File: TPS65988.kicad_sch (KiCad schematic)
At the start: 30 parts, among them J10 USB_C_Receptacle, J11 Conn_01x03, J12 Conn_01x03, J13 Conn_01x04, J9 USB_C_Receptacle, U13 TPS65988

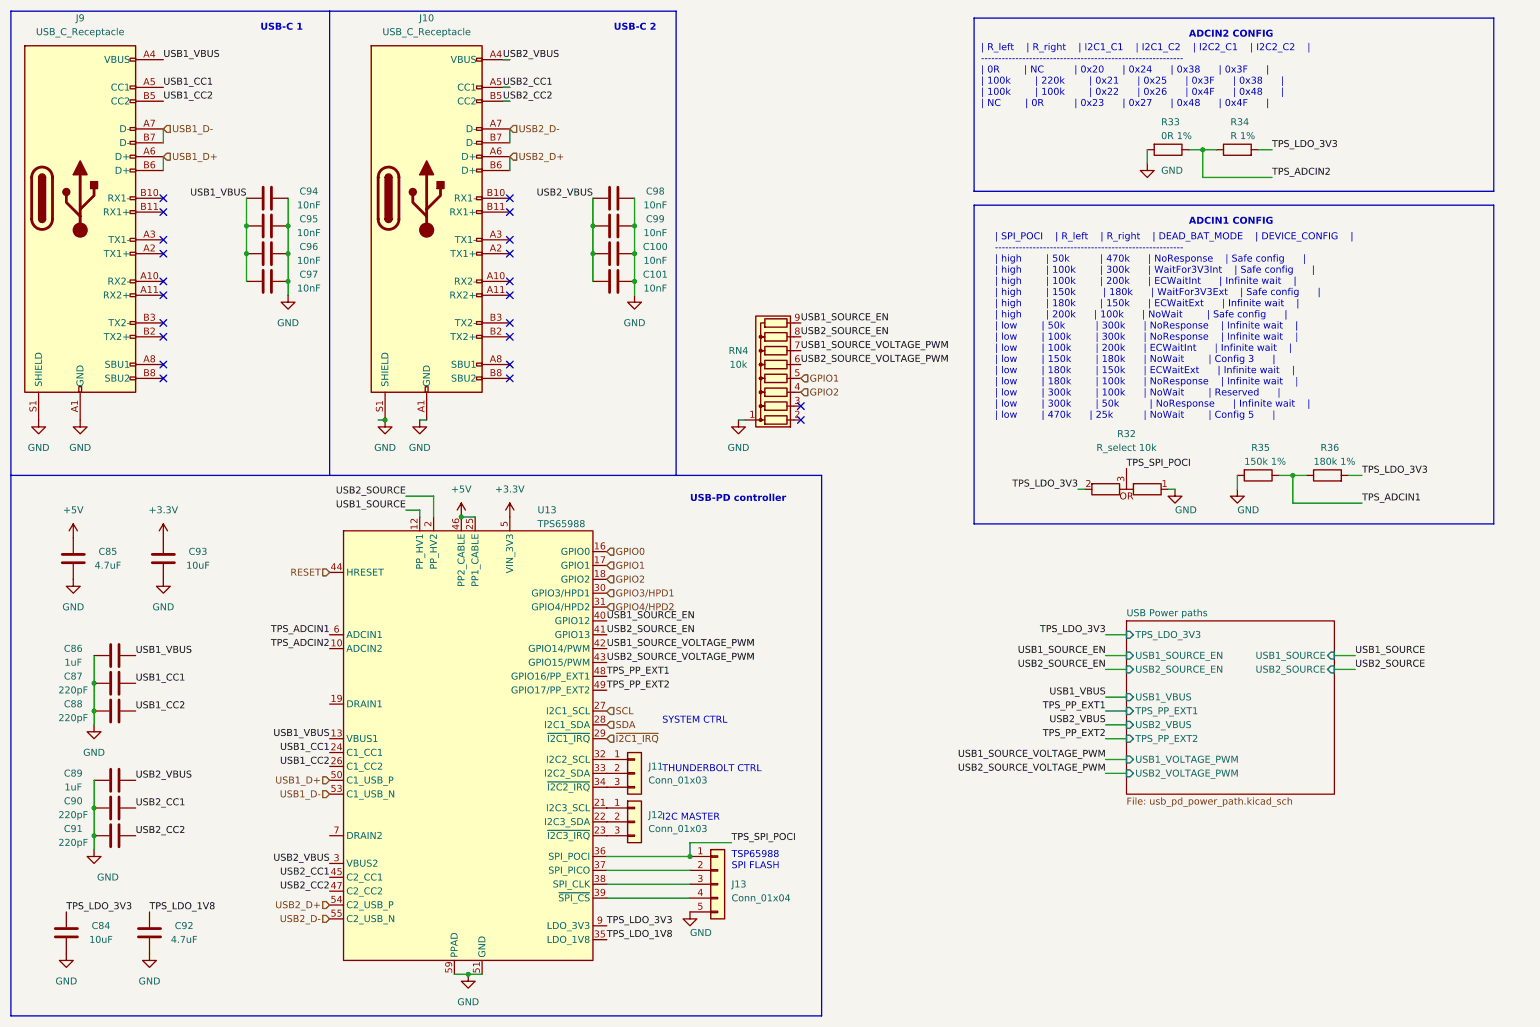
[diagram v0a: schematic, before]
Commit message: added nfc antenna components, added most of footprints
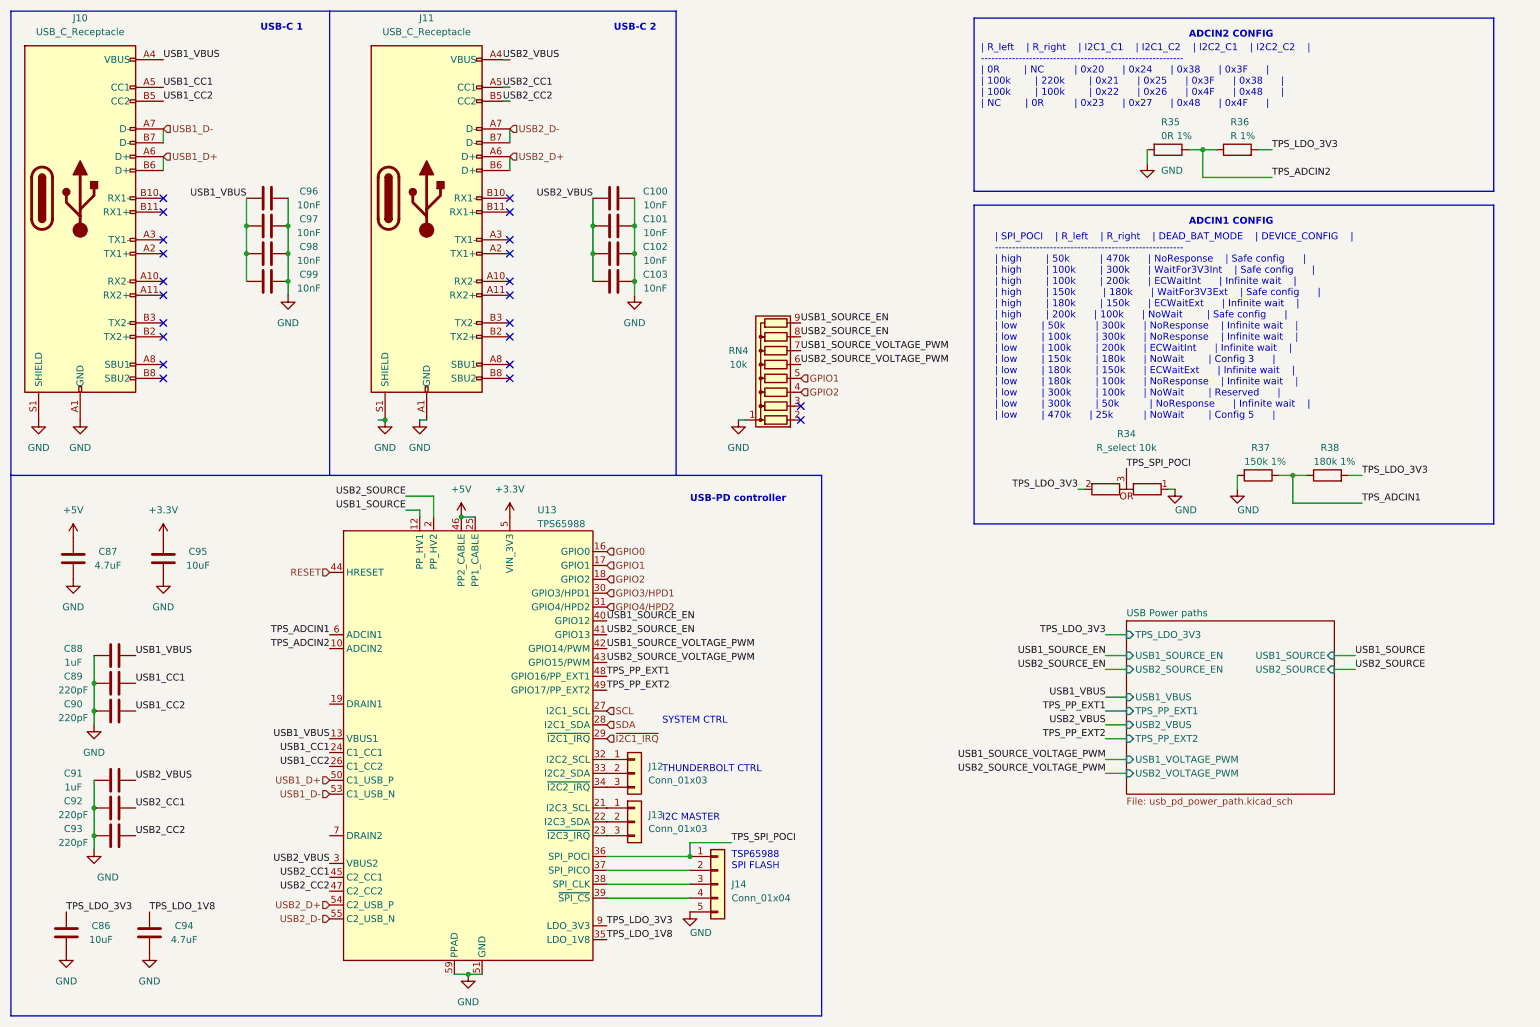
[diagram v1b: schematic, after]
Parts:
- C100: renamed from C98; footprint (none) -> Capacitor_SMD:C_0603_1608Metric_Pad1.08x0.95mm_HandSolder
- C101: renamed from C99; footprint (none) -> Capacitor_SMD:C_0603_1608Metric_Pad1.08x0.95mm_HandSolder
- C102: renamed from C100; footprint (none) -> Capacitor_SMD:C_0603_1608Metric_Pad1.08x0.95mm_HandSolder
- C103: renamed from C101; footprint (none) -> Capacitor_SMD:C_0603_1608Metric_Pad1.08x0.95mm_HandSolder
- C87: renamed from C85; footprint (none) -> Capacitor_SMD:C_0603_1608Metric_Pad1.08x0.95mm_HandSolder
- C88: renamed from C86; footprint (none) -> Capacitor_SMD:C_0603_1608Metric_Pad1.08x0.95mm_HandSolder
- C89: renamed from C87; footprint (none) -> Capacitor_SMD:C_0603_1608Metric_Pad1.08x0.95mm_HandSolder
- C90: renamed from C88; footprint (none) -> Capacitor_SMD:C_0603_1608Metric_Pad1.08x0.95mm_HandSolder
- C91: renamed from C89; footprint (none) -> Capacitor_SMD:C_0603_1608Metric_Pad1.08x0.95mm_HandSolder
- C92: renamed from C90; footprint (none) -> Capacitor_SMD:C_0603_1608Metric_Pad1.08x0.95mm_HandSolder
- C93: renamed from C91; footprint (none) -> Capacitor_SMD:C_0603_1608Metric_Pad1.08x0.95mm_HandSolder
- C94: renamed from C92; footprint (none) -> Capacitor_SMD:C_0603_1608Metric_Pad1.08x0.95mm_HandSolder
- C96: renamed from C94; footprint (none) -> Capacitor_SMD:C_0603_1608Metric_Pad1.08x0.95mm_HandSolder
- C97: renamed from C95; footprint (none) -> Capacitor_SMD:C_0603_1608Metric_Pad1.08x0.95mm_HandSolder
- C98: renamed from C96; footprint (none) -> Capacitor_SMD:C_0603_1608Metric_Pad1.08x0.95mm_HandSolder
- C99: renamed from C97; footprint (none) -> Capacitor_SMD:C_0603_1608Metric_Pad1.08x0.95mm_HandSolder
- J10: renamed from J9; footprint (none) -> airsoft_controller:USB-C-2305018-2
- J11: renamed from J10; footprint (none) -> airsoft_controller:USB-C-2305018-2
- J12: renamed from J11; footprint (none) -> Connector_PinSocket_2.54mm:PinSocket_1x03_P2.54mm_Vertical
- J13: renamed from J12; footprint (none) -> Connector_PinSocket_2.54mm:PinSocket_1x03_P2.54mm_Vertical
- J14: renamed from J13; footprint (none) -> Connector_PinSocket_2.54mm:PinSocket_1x04_P2.54mm_Vertical
- R34: renamed from R32; footprint (none) -> airsoft_controller:0603-R-select
- R36: renamed from R34; footprint (none) -> Resistor_SMD:R_0603_1608Metric_Pad0.98x0.95mm_HandSolder
- R37: renamed from R35; footprint (none) -> Resistor_SMD:R_0603_1608Metric_Pad0.98x0.95mm_HandSolder
- R38: renamed from R36; footprint (none) -> Resistor_SMD:R_0603_1608Metric_Pad0.98x0.95mm_HandSolder
- U13: footprint (none) -> airsoft_controller:VQFN-56-3EP
- renumbered C84 to C86, C93 to C95, R33 to R35

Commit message: schematic creation
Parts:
- added C104, C98: 0.1uF, Capacitor_SMD:C_0603_1608Metric_Pad1.08x0.95mm_HandSolder, symbol Device:C
- added C105, C99: 1uF, Capacitor_SMD:C_0603_1608Metric_Pad1.08x0.95mm_HandSolder, symbol Device:C
- added J10, J15: Conn_01x01, Connector_PinSocket_2.54mm:PinSocket_1x01_P2.54mm_Vertical, symbol Connector_Generic:Conn_01x01
- added R32, R33: 100k, Resistor_SMD:R_0603_1608Metric_Pad0.98x0.95mm_HandSolder, symbol Device:R
- added U13, U15: TPD6S300A, Package_DFN_QFN:WQFN-20-1EP_3x3mm_P0.4mm_EP1.7x1.7mm, symbol airsoft_controller:TPD6S300A
- C88: renamed from C86; footprint (none) -> Capacitor_SMD:C_1206_3216Metric_Pad1.33x1.80mm_HandSolder
- C97: renamed from C95; footprint (none) -> Capacitor_SMD:C_1206_3216Metric_Pad1.33x1.80mm_HandSolder
- J14: value Conn_01x04 -> Conn_01x05; footprint Connector_PinSocket_2.54mm:PinSocket_1x04_P2.54mm_Vertical -> Connector_PinSocket_2.54mm:PinSocket_1x05_P2.54mm_Vertical
- R35: footprint (none) -> Resistor_SMD:R_0603_1608Metric_Pad0.98x0.95mm_HandSolder
- renumbered C96 to C100, C97 to C101, C98 to C102, C99 to C103, C100 to C106, C101 to C107, C102 to C108, C103 to C109, C87 to C89, C88 to C90, C89 to C91, C90 to C92, C91 to C93, C92 to C94, C93 to C95, C94 to C96, J10 to J9, U13 to U14
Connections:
- net +3.3V: now also C105.2, C99.2, R32.2, R33.2, U13.10 (VPWR), U15.10 (VPWR)
- net GND: now also C104.1, C105.1, C98.1, C99.1, U13.13 (GND), U13.18 (GND), U13.21 (PAD), U13.8 (GND), U15.13 (GND), U15.18 (GND), U15.21 (PAD), U15.8 (GND)
- net USB1_CC1: now also U13.12 (CC1), U13.7 (RPD_G1); no longer J9.A5 (CC1)
- net USB1_CC2: now also U13.11 (CC2), U13.6 (RPD_G2); no longer J9.B5 (CC2)
- net USB1_D+: now also U13.20 (D1)
- net USB1_D-: now also U13.19 (D2)
- net USB2_CC1: now also U15.12 (CC1), U15.7 (RPD_G1); no longer J11.A5 (CC1)
- net USB2_CC2: now also U15.11 (CC2), U15.6 (RPD_G2); no longer J11.B5 (CC2)
- net USB2_D+: now also U15.20 (D1)
- net USB2_D-: now also U15.19 (D2)
- net USB1_C_SBU1: now reaches J9.A8 (SBU1)
- net USB1_C_SBU1: now also U13.1 (C_SBU1)
- net USB1_C_SBU2: now reaches J9.B8 (SBU2)
- net USB1_C_SBU2: now also U13.2 (C_SBU2)
- net USB2_C_SBU1: now reaches J11.A8 (SBU1)
- net USB2_C_SBU1: now also U15.1 (C_SBU1)
- net USB2_C_SBU2: now reaches J11.B8 (SBU2)
- net USB2_C_SBU2: now also U15.2 (C_SBU2)
- new net: C104.2, U15.3 (VBIAS)
- new net: J15.1 (Pin_1), R33.1, U15.9 (~{FLT})
- new net: C98.2, U13.3 (VBIAS)
- new net: J10.1 (Pin_1), R32.1, U13.9 (~{FLT})
- new net USB1_C_CC1: J9.A5 (CC1), U13.4 (C_CC1)
- new net USB1_C_CC2: J9.B5 (CC2), U13.5 (C_CC2)
- new net USB2_C_CC1: J11.A5 (CC1), U15.4 (C_CC1)
- new net USB2_C_CC2: J11.B5 (CC2), U15.5 (C_CC2)
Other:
- moved on the sheet: C100, C101, C102, C103, C106, C107, C108, C109, J11, RN4

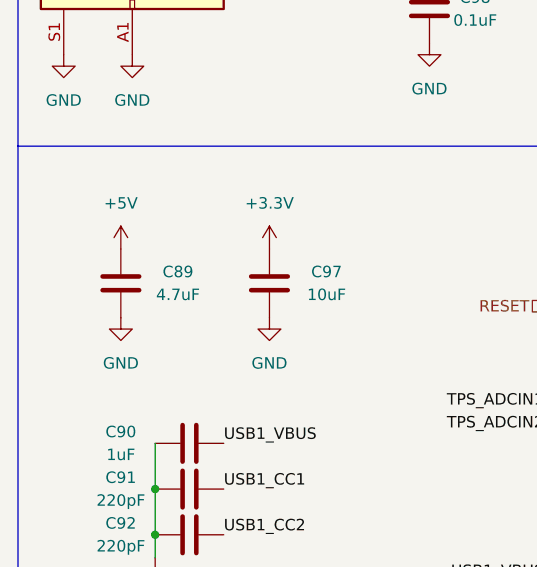
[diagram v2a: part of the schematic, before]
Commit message: edited usb pcb part
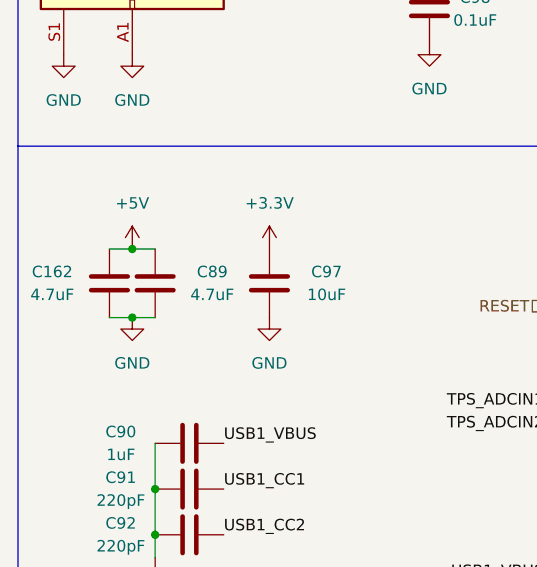
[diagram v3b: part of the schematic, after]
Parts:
- added C162: 4.7uF, Capacitor_SMD:C_0603_1608Metric_Pad1.08x0.95mm_HandSolder, symbol Device:C
- C88, C97: footprint Capacitor_SMD:C_1206_3216Metric_Pad1.33x1.80mm_HandSolder -> Capacitor_SMD:C_0805_2012Metric_Pad1.18x1.45mm_HandSolder
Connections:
- net +5V: now also C162.2
- net GND: now also C162.1
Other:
- moved on the sheet: C89
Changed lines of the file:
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@@
   (junction (at 86.36 60.96) (diameter 0) (color 0 0 0 0)
   )
+  (junction (at 25.4 116.84) (diameter 0) (color 0 0 0 0)
+  )
   (junction (at 176.53 29.21) (diameter 0) (color 0 0 0 0)
   )
@@
   )
   (junction (at 168.91 29.21) (diameter 0) (color 0 0 0 0)
+  )
+  (junction (at 25.4 109.22) (diameter 0) (color 0 0 0 0)
   )
   (junction (at 27.94 140.97) (diameter 0) (color 0 0 0 0)
@@
     (stroke (width 0) (type default) (color 0 0 0 0))
   )
+  (wire (pts (xy 25.4 116.84) (xy 27.94 116.84))
+    (stroke (width 0) (type default) (color 0 0 0 0))
+  )
   (wire (pts (xy 213.36 140.97) (xy 217.17 140.97))
     (stroke (width 0) (type default) (color 0 0 0 0))
@@
     (stroke (width 0) (type default) (color 0 0 0 0))
   )
+  (wire (pts (xy 22.86 116.84) (xy 25.4 116.84))
+    (stroke (width 0) (type default) (color 0 0 0 0))
+  )
+  (wire (pts (xy 22.86 109.22) (xy 25.4 109.22))
+    (stroke (width 0) (type default) (color 0 0 0 0))
+  )
   (wire (pts (xy 146.05 78.74) (xy 151.13 78.74))
+    (stroke (width 0) (type default) (color 0 0 0 0))
+  )
+  (wire (pts (xy 25.4 109.22) (xy 27.94 109.22))
     (stroke (width 0) (type default) (color 0 0 0 0))
   )
@@
     (pin "1")
   )
-  (symbol (lib_id "power:GND") (at 24.13 116.84 0) (unit 1)
-    (in_bom yes) (on_board yes) (fields_autoplaced)
-    (property "Reference" "#PWR0105" (id 0) (at 24.13 123.19 0)
-      (effects (font (size 1.27 1.27)) hide)
-    )
-    (property "Value" "GND" (id 1) (at 24.13 121.92 0))
-    (property "Footprint" "" (id 2) (at 24.13 116.84 0)
-      (effects (font (size 1.27 1.27)) hide)
-    )
-    (property "Datasheet" "" (id 3) (at 24.13 116.84 0)
+  (symbol (lib_id "power:GND") (at 25.4 116.84 0) (unit 1)
+    (in_bom yes) (on_board yes) (fields_autoplaced)
+    (property "Reference" "#PWR0105" (id 0) (at 25.4 123.19 0)
+      (effects (font (size 1.27 1.27)) hide)
+    )
+    (property "Value" "GND" (id 1) (at 25.4 121.92 0))
+    (property "Footprint" "" (id 2) (at 25.4 116.84 0)
+      (effects (font (size 1.27 1.27)) hide)
+    )
+    (property "Datasheet" "" (id 3) (at 25.4 116.84 0)
       (effects (font (size 1.27 1.27)) hide)
     )
@@
     )
     (pin "1")
+  )
+  (symbol (lib_id "Device:C") (at 22.86 113.03 180) (unit 1)
+    (in_bom yes) (on_board yes)
+    (property "Reference" "C162" (id 0) (at 16.51 111.76 0))
+    (property "Value" "4.7uF" (id 1) (at 16.51 114.3 0))
+    (property "Footprint" "Capacitor_SMD:C_0603_1608Metric_Pad1.08x0.95mm_HandSolder" (id 2) (at 21.8948 109.22 0)
+      (effects (font (size 1.27 1.27)) hide)
+    )
+    (property "Datasheet" "~" (id 3) (at 22.86 113.03 0)
+      (effects (font (size 1.27 1.27)) hide)
+    )
+    (pin "1")
+    (pin "2")
   )
   (symbol (lib_id "Device:C") (at 38.1 181.61 180) (unit 1)
@@
     (property "Reference" "C97" (id 0) (at 46.99 111.76 0))
     (property "Value" "10uF" (id 1) (at 46.99 114.3 0))
-    (property "Footprint" "Capacitor_SMD:C_1206_3216Metric_Pad1.33x1.80mm_HandSolder" (id 2) (at 39.6748 109.22 0)
+    (property "Footprint" "Capacitor_SMD:C_0805_2012Metric_Pad1.18x1.45mm_HandSolder" (id 2) (at 39.6748 109.22 0)
       (effects (font (size 1.27 1.27)) hide)
     )
@@
     (pin "1")
   )
-  (symbol (lib_id "power:+5V") (at 24.13 109.22 0) (unit 1)
-    (in_bom yes) (on_board yes) (fields_autoplaced)
-    (property "Reference" "#PWR0104" (id 0) (at 24.13 113.03 0)
-      (effects (font (size 1.27 1.27)) hide)
-    )
-    (property "Value" "+5V" (id 1) (at 24.13 104.14 0))
-    (property "Footprint" "" (id 2) (at 24.13 109.22 0)
-      (effects (font (size 1.27 1.27)) hide)
-    )
-    (property "Datasheet" "" (id 3) (at 24.13 109.22 0)
+  (symbol (lib_id "power:+5V") (at 25.4 109.22 0) (unit 1)
+    (in_bom yes) (on_board yes) (fields_autoplaced)
+    (property "Reference" "#PWR0104" (id 0) (at 25.4 113.03 0)
+      (effects (font (size 1.27 1.27)) hide)
+    )
+    (property "Value" "+5V" (id 1) (at 25.4 104.14 0))
+    (property "Footprint" "" (id 2) (at 25.4 109.22 0)
+      (effects (font (size 1.27 1.27)) hide)
+    )
+    (property "Datasheet" "" (id 3) (at 25.4 109.22 0)
       (effects (font (size 1.27 1.27)) hide)
     )
@@
     (pin "1")
   )
-  (symbol (lib_id "Device:C") (at 24.13 113.03 180) (unit 1)
-    (in_bom yes) (on_board yes)
-    (property "Reference" "C89" (id 0) (at 30.48 111.76 0))
-    (property "Value" "4.7uF" (id 1) (at 30.48 114.3 0))
-    (property "Footprint" "Capacitor_SMD:C_0603_1608Metric_Pad1.08x0.95mm_HandSolder" (id 2) (at 23.1648 109.22 0)
-      (effects (font (size 1.27 1.27)) hide)
-    )
-    (property "Datasheet" "~" (id 3) (at 24.13 113.03 0)
+  (symbol (lib_id "Device:C") (at 27.94 113.03 180) (unit 1)
+    (in_bom yes) (on_board yes)
+    (property "Reference" "C89" (id 0) (at 34.29 111.76 0))
+    (property "Value" "4.7uF" (id 1) (at 34.29 114.3 0))
+    (property "Footprint" "Capacitor_SMD:C_0603_1608Metric_Pad1.08x0.95mm_HandSolder" (id 2) (at 26.9748 109.22 0)
+      (effects (font (size 1.27 1.27)) hide)
+    )
+    (property "Datasheet" "~" (id 3) (at 27.94 113.03 0)
       (effects (font (size 1.27 1.27)) hide)
     )
@@
     (property "Reference" "C88" (id 0) (at 29.21 180.34 0))
     (property "Value" "10uF" (id 1) (at 29.21 182.88 0))
-    (property "Footprint" "Capacitor_SMD:C_1206_3216Metric_Pad1.33x1.80mm_HandSolder" (id 2) (at 21.8948 177.8 0)
-      (effects (font (size 1.27 1.27)) hide)
-    )
+    (property "Footprint" "Capacitor_SMD:C_0805_2012Metric_Pad1.18x1.45mm_HandSolder" (id 2) (at 21.8948 177.8 0)
+      (effects (font (size 1.27 1.27)) hide)
+    )
